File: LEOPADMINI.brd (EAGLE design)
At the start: 74 x 110 mm, 47 parts, among them IC1 ATMEGA32U4-QFN

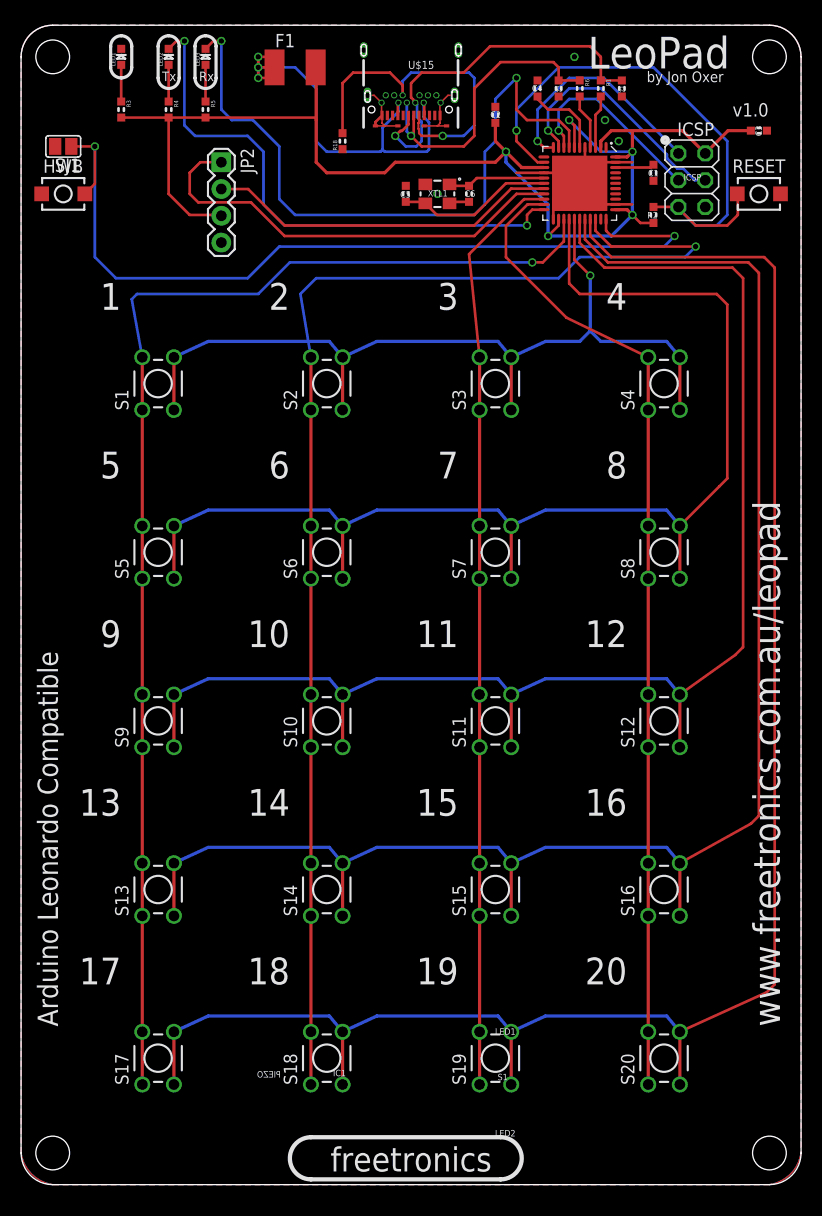
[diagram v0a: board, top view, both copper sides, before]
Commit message: Resized to suit 6mm tact switches
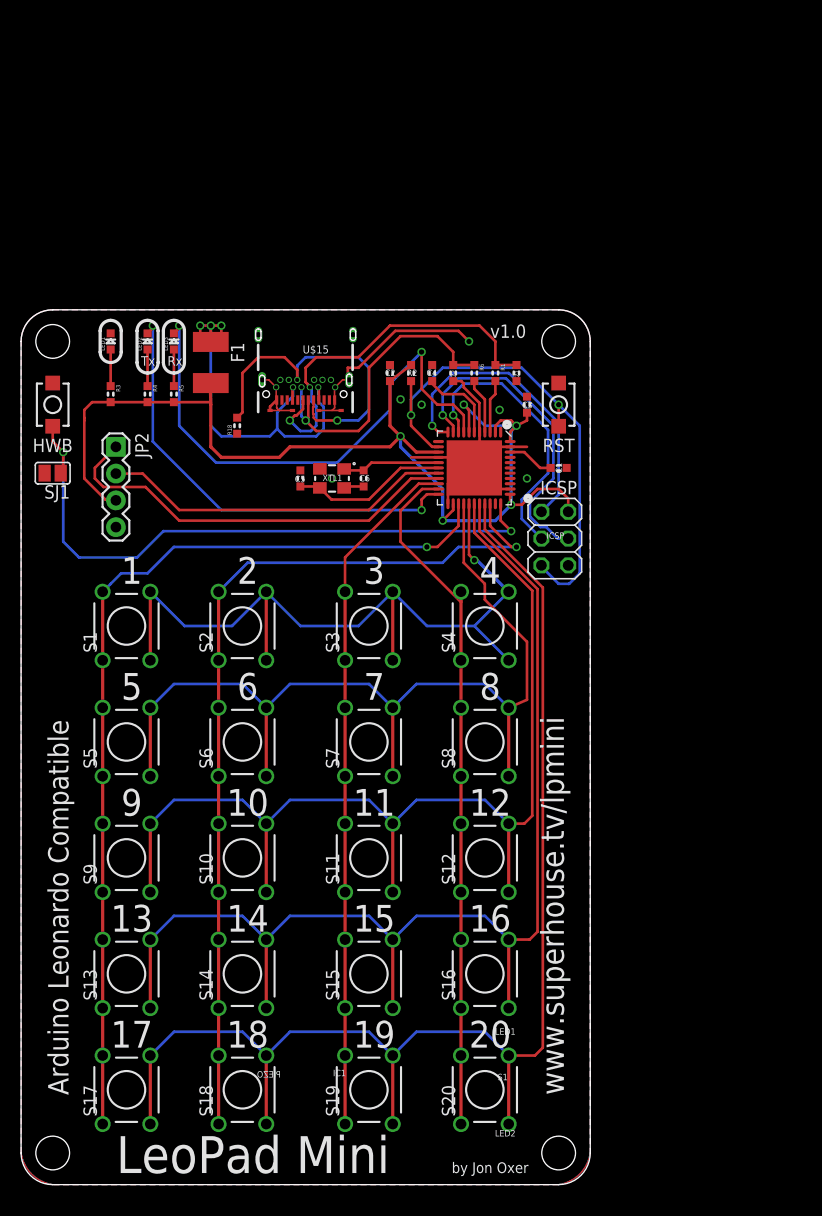
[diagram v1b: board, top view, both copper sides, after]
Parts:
- S1, S10, S11, S12, S13, S14, S15, S16, S17, S18, S19, S2, S20, S3, S4, S5, S6, S7, S8, S9: device freetronics-jon:TACTILE-PTH-4.5MM -> freetronics-original:TACTILE-PTH
- moved ICSP 36.4 mm to (50.6, 61.3)
- moved C3 34.1 mm to (48.0, 74.0), turned to 90 degrees
- moved SJ1 31.0 mm to (3.00, 67.5)
- moved C1 29.4 mm to (51.0, 68.0), turned to 0 degrees
- moved F1 29.1 mm to (18.0, 78.0), turned to 270 degrees
- moved C4 28.8 mm to (39.0, 77.0)
- moved C5 28.8 mm to (26.5, 67.0)
- moved C6 28.8 mm to (32.5, 67.0)
- moved IC1 28.8 mm to (43.0, 68.0)
- moved JP2 28.8 mm to (9.00, 70.0)
- moved R1 28.8 mm to (45.0, 77.0)
- moved R18 28.8 mm to (20.5, 72.0)
- moved R6 28.8 mm to (43.0, 77.0)
- moved U$15 28.8 mm to (30.6, 75.0)
- moved XTL1 28.8 mm to (29.5, 67.0)
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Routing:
- net ROW4: track 169.6 -> 123.0 mm
- net COL1: track 125.7 -> 86.0 mm
- net ROW3: track 151.1 -> 111.5 mm
- net ROW2: track 132.7 -> 100.0 mm
- net COL0: track 120.0 -> 88.9 mm
- net ROW1: track 115.9 -> 88.6 mm
- net COL3: track 93.1 -> 67.0 mm
- net COL2: track 88.1 -> 65.5 mm
- net HWB: track 82.9 -> 60.6 mm
- net GND: track 40.6 -> 59.9 mm, vias 4 -> 6
- net 5V: track 129.1 -> 111.1 mm
- net RXLED_SS: track 64.5 -> 51.2 mm
- net TX_LED: track 52.0 -> 43.3 mm
- net SCK: track 18.8 -> 27.2 mm
- net MOSI: track 23.7 -> 31.2 mm
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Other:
- board size 74 x 110 mm -> 54 x 83 mm
- board text added: "Copyright 2018 SuperHouse Automation Pty Ltd Released under the TAPR Open Hardware License www.tapr.org/OHL"
- board text added: "D2/SDA"
- board text added: "D3/SCL"
- board text added: "LeoPad Mini"
- board text added: "RST"
- board text added: "Super House"
- board text added: "USB-C"
- board text added: "www.superhouse.tv/lpmini"
- board text removed: "Copyright 2018 Freetronics Pty Ltd Released under the TAPR Open Hardware License www.tapr.org/OHL"
- board text removed: "D2 (SDA)"
- board text removed: "D3 (SCL)"
- board text removed: "LeoPad"
- board text removed: "RESET"
- board text removed: "freetronics"
- board text removed: "www.freetronics.com.au/leopad"
